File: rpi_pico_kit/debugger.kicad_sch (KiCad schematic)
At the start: 43 parts, among them J2 USB_B, U2 NCP1117-3.3_SOT223, U3 RP2040, U4 W25Q16JVSSIQ, U5 74HC14, Y1 12MHz

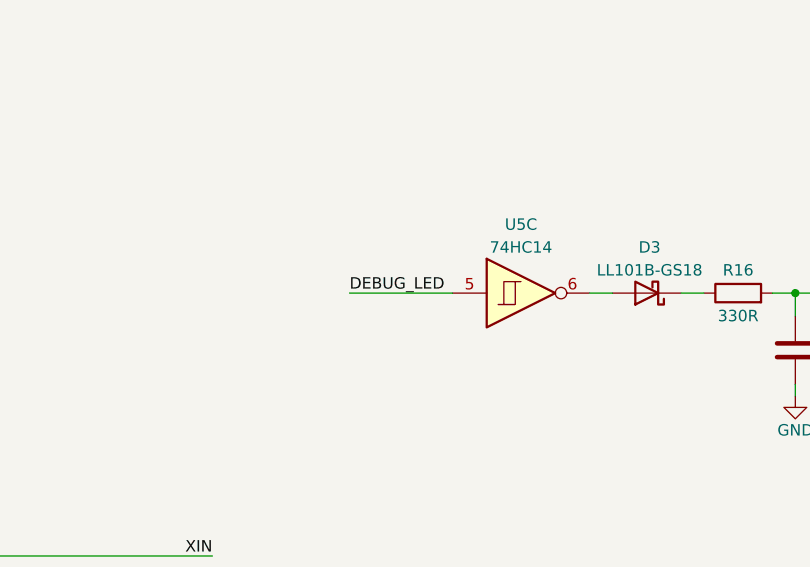
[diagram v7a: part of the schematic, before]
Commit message: changed pinout
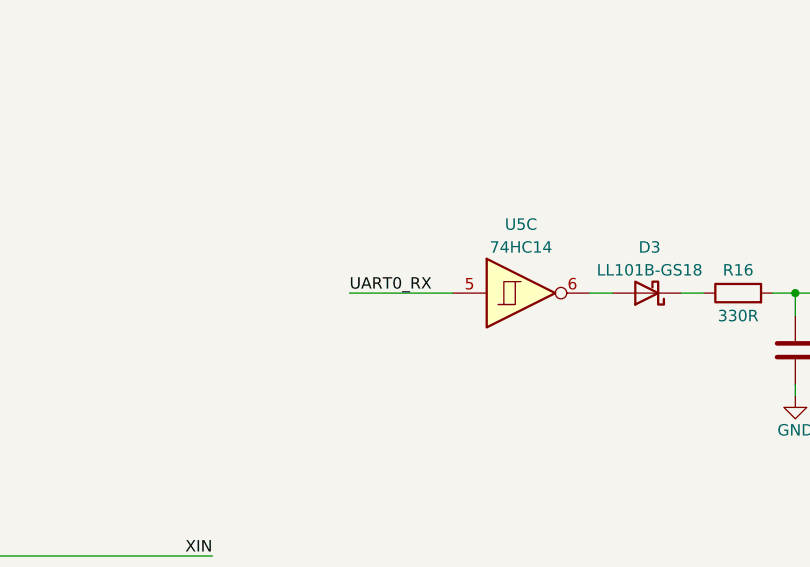
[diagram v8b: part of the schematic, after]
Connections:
- net DEBUG_LED: no longer U5.5
- new net UART0_RX: U5.5
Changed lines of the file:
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@@
     (effects (font (size 1.27 1.27)) (justify right bottom))
   )
-  (label "DEBUG_LED" (at 181.61 142.24 0) (fields_autoplaced)
+  (label "UART0_RX" (at 181.61 142.24 0) (fields_autoplaced)
     (effects (font (size 1.27 1.27)) (justify left bottom))
   )
